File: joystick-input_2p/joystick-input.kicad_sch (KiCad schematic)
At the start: 16 parts, among them J1 Conn_01x18, J2 Conn_02x14_Odd_Even

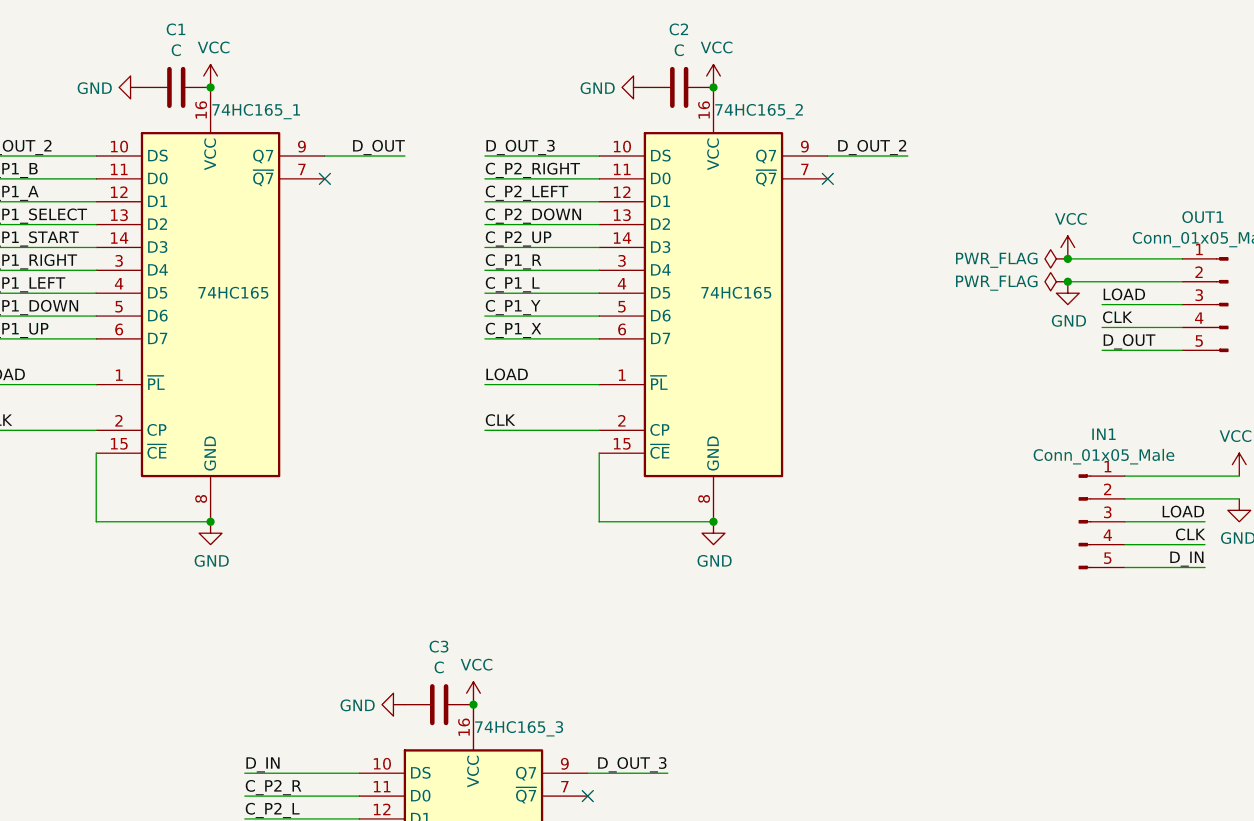
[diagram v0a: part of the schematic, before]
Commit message: joystick-input_2p 스크린샷
Signed-off-by: Ju, Gyeong-min <jcmh74@gmail.com>
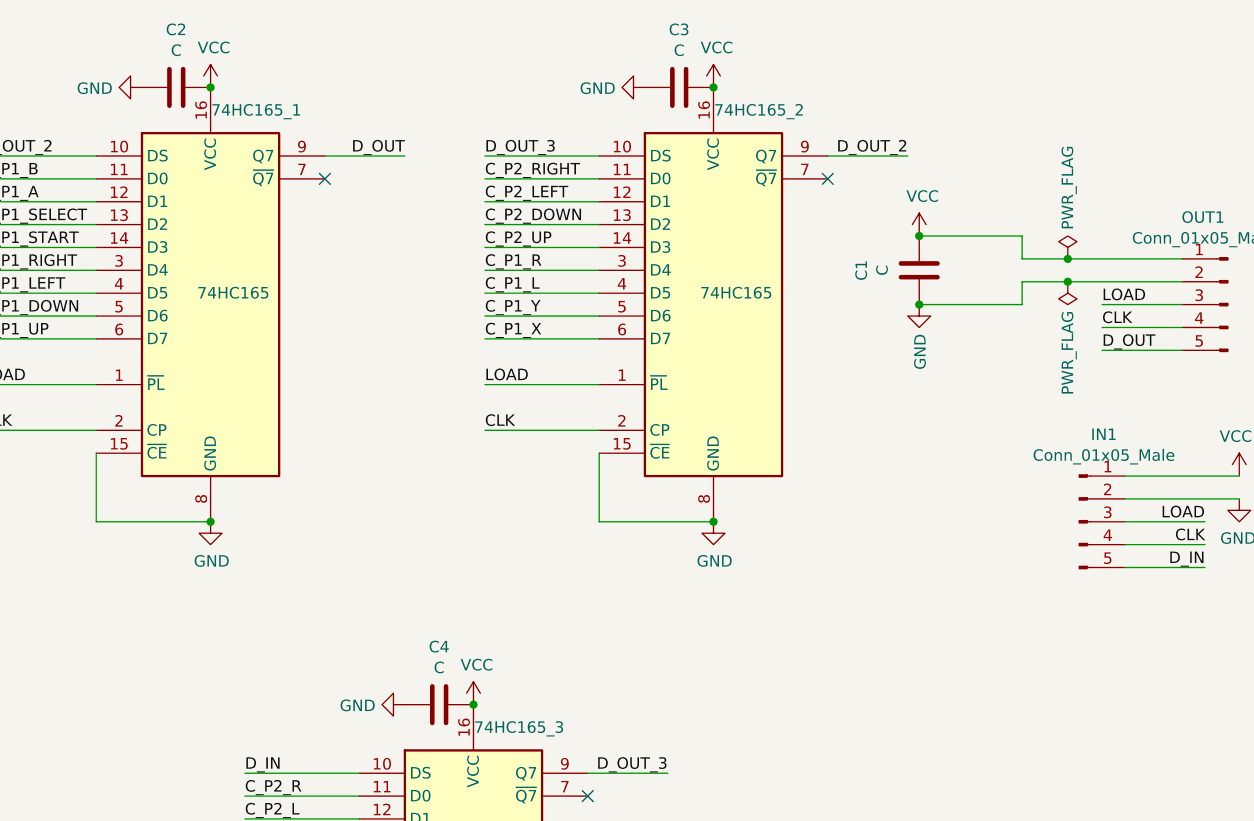
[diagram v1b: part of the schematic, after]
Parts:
- added C1: C, Capacitor_SMD:C_0805_2012Metric_Pad1.18x1.45mm_HandSolder, symbol Device:C
- renumbered C1 to C2, C2 to C3, C3 to C4
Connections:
- net GND: now also C1.2
- net VCC: now also C1.1

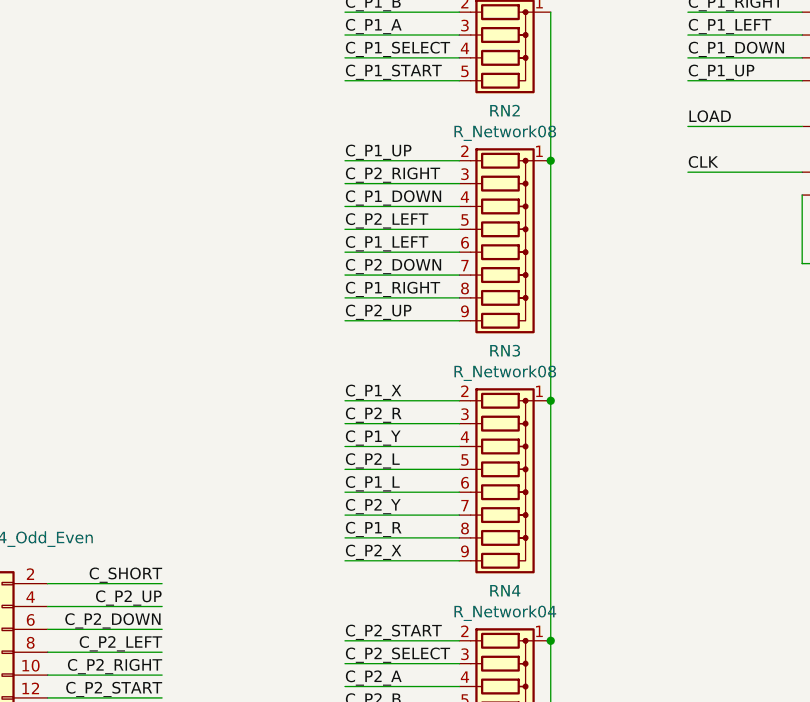
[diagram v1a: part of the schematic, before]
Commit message: 74hc165 board array-resistance change
Signed-off-by: Ju, Gyeong-min <jcmh74@gmail.com>
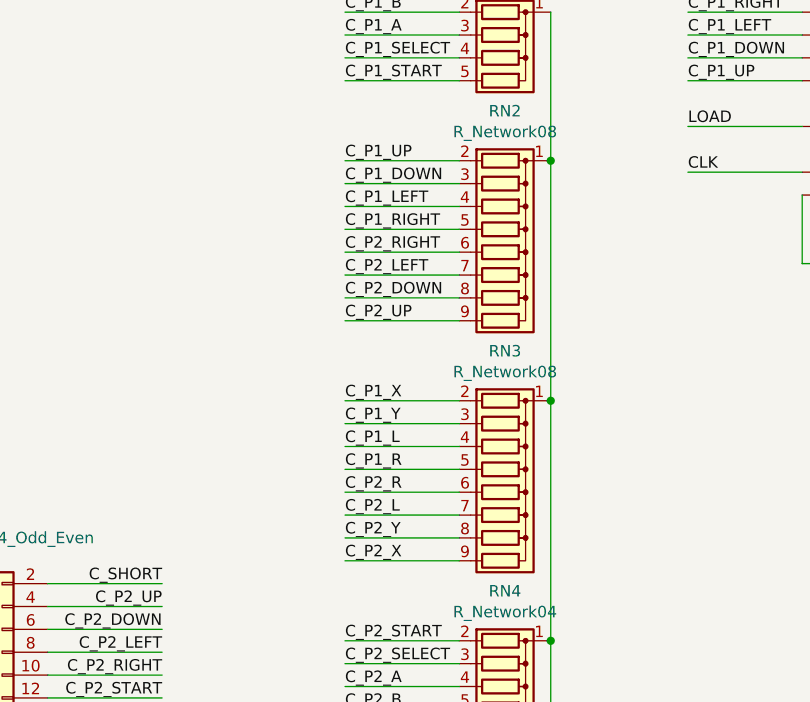
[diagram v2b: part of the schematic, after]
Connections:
- net C_P1_DOWN: now also RN2.3 (R2); no longer RN2.4 (R3)
- net C_P1_L: now also RN3.4 (R3); no longer RN3.6 (R5)
- net C_P1_LEFT: now also RN2.4 (R3); no longer RN2.6 (R5)
- net C_P1_R: now also RN3.5 (R4); no longer RN3.8 (R7)
- net C_P1_RIGHT: now also RN2.5 (R4); no longer RN2.8 (R7)
- net C_P1_Y: now also RN3.3 (R2); no longer RN3.4 (R3)
- net C_P2_DOWN: now also RN2.8 (R7); no longer RN2.7 (R6)
- net C_P2_L: now also RN3.7 (R6); no longer RN3.5 (R4)
- net C_P2_LEFT: now also RN2.7 (R6); no longer RN2.5 (R4)
- net C_P2_R: now also RN3.6 (R5); no longer RN3.3 (R2)
- net C_P2_RIGHT: now also RN2.6 (R5); no longer RN2.3 (R2)
- net C_P2_Y: now also RN3.8 (R7); no longer RN3.7 (R6)
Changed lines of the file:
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@@
     (effects (font (size 1.27 1.27)) (justify left bottom))
   )
-  (label "C_P1_R" (at 85.09 115.57 0)
+  (label "C_P1_R" (at 85.09 107.95 0)
     (effects (font (size 1.27 1.27)) (justify left bottom))
   )
@@
     (effects (font (size 1.27 1.27)) (justify left bottom))
   )
-  (label "C_P1_DOWN" (at 85.09 78.74 0)
+  (label "C_P1_DOWN" (at 85.09 76.2 0)
     (effects (font (size 1.27 1.27)) (justify left bottom))
   )
@@
     (effects (font (size 1.27 1.27)) (justify right bottom))
   )
-  (label "C_P2_RIGHT" (at 85.09 76.2 0)
-    (effects (font (size 1.27 1.27)) (justify left bottom))
-  )
-  (label "C_P1_Y" (at 85.09 105.41 0)
+  (label "C_P2_RIGHT" (at 85.09 83.82 0)
+    (effects (font (size 1.27 1.27)) (justify left bottom))
+  )
+  (label "C_P1_Y" (at 85.09 102.87 0)
     (effects (font (size 1.27 1.27)) (justify left bottom))
   )
@@
     (effects (font (size 1.27 1.27)) (justify left bottom))
   )
-  (label "C_P1_L" (at 85.09 110.49 0)
+  (label "C_P1_L" (at 85.09 105.41 0)
     (effects (font (size 1.27 1.27)) (justify left bottom))
   )
@@
     (effects (font (size 1.27 1.27)) (justify left bottom))
   )
-  (label "C_P2_LEFT" (at 85.09 81.28 0)
+  (label "C_P2_LEFT" (at 85.09 86.36 0)
     (effects (font (size 1.27 1.27)) (justify left bottom))
   )
@@
     (effects (font (size 1.27 1.27)) (justify left bottom))
   )
-  (label "C_P2_L" (at 85.09 107.95 0)
-    (effects (font (size 1.27 1.27)) (justify left bottom))
-  )
-  (label "C_P1_RIGHT" (at 85.09 88.9 0)
+  (label "C_P2_L" (at 85.09 113.03 0)
+    (effects (font (size 1.27 1.27)) (justify left bottom))
+  )
+  (label "C_P1_RIGHT" (at 85.09 81.28 0)
     (effects (font (size 1.27 1.27)) (justify left bottom))
   )
@@
     (effects (font (size 1.27 1.27)) (justify right bottom))
   )
-  (label "C_P1_LEFT" (at 85.09 83.82 0)
+  (label "C_P1_LEFT" (at 85.09 78.74 0)
     (effects (font (size 1.27 1.27)) (justify left bottom))
   )
@@
     (effects (font (size 1.27 1.27)) (justify right bottom))
   )
-  (label "C_P2_Y" (at 85.09 113.03 0)
+  (label "C_P2_Y" (at 85.09 115.57 0)
     (effects (font (size 1.27 1.27)) (justify left bottom))
   )
@@
     (effects (font (size 1.27 1.27)) (justify left bottom))
   )
-  (label "C_P2_R" (at 85.09 102.87 0)
+  (label "C_P2_R" (at 85.09 110.49 0)
     (effects (font (size 1.27 1.27)) (justify left bottom))
   )
@@
     (effects (font (size 1.27 1.27)) (justify right bottom))
   )
-  (label "C_P2_DOWN" (at 85.09 86.36 0)
-    (effects (font (size 1.27 1.27)) (justify left bottom))
-  )
+  (label "C_P2_DOWN" (at 85.09 88.9 0)
+    (effects (font (size 1.27 1.27)) (justify left bottom))
+  )

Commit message: 도면 시트 설명 추가
Signed-off-by: Ju, Gyeong-min <jcmh74@gmail.com>
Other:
- company: (none) -> Amos Home
- title: (none) -> Joystick Input Board (2P)
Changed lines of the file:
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@@
 (kicad_sch (version 20211123) (generator eeschema)
   (paper "A4")
+  (title_block
+    (title "Joystick Input Board (2P)")
+    (rev "4")
+    (company "Amos Home")
+  )
   (junction (at 177.8 153.67) (diameter 0) (color 0 0 0 0)
   )
